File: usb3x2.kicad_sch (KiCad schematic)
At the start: 102 parts, among them J501 WE_632723300011_alt_symbol, J502 WE_632723300011_alt_symbol, Q501 BSS138W-7-F, Q502 BSS138W-7-F, U501 HD3SS3220, U502 HD3SS3220, U503 AP22615, U504 AP22615, U505 TPD4E05U06QDQARQ1, U506 TPD4E05U06QDQARQ1, U507 TPD4E05U06QDQARQ1, U508 TPD4E05U06QDQARQ1, U509 TPD4E05U06QDQARQ1, U510 TPD4E05U06QDQARQ1

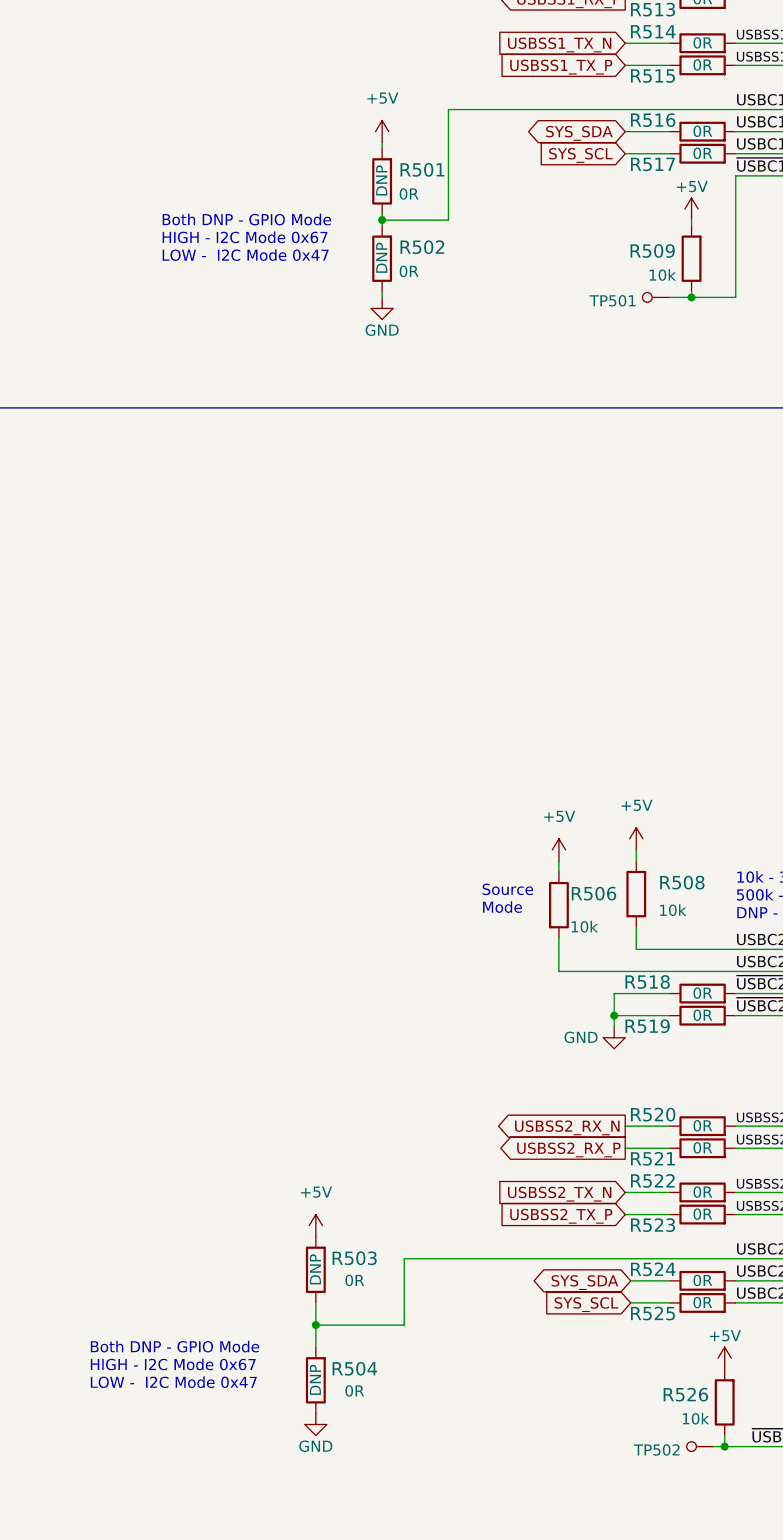
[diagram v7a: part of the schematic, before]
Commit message: Cleaned up the schematic, fixed library issues, annotated schematic
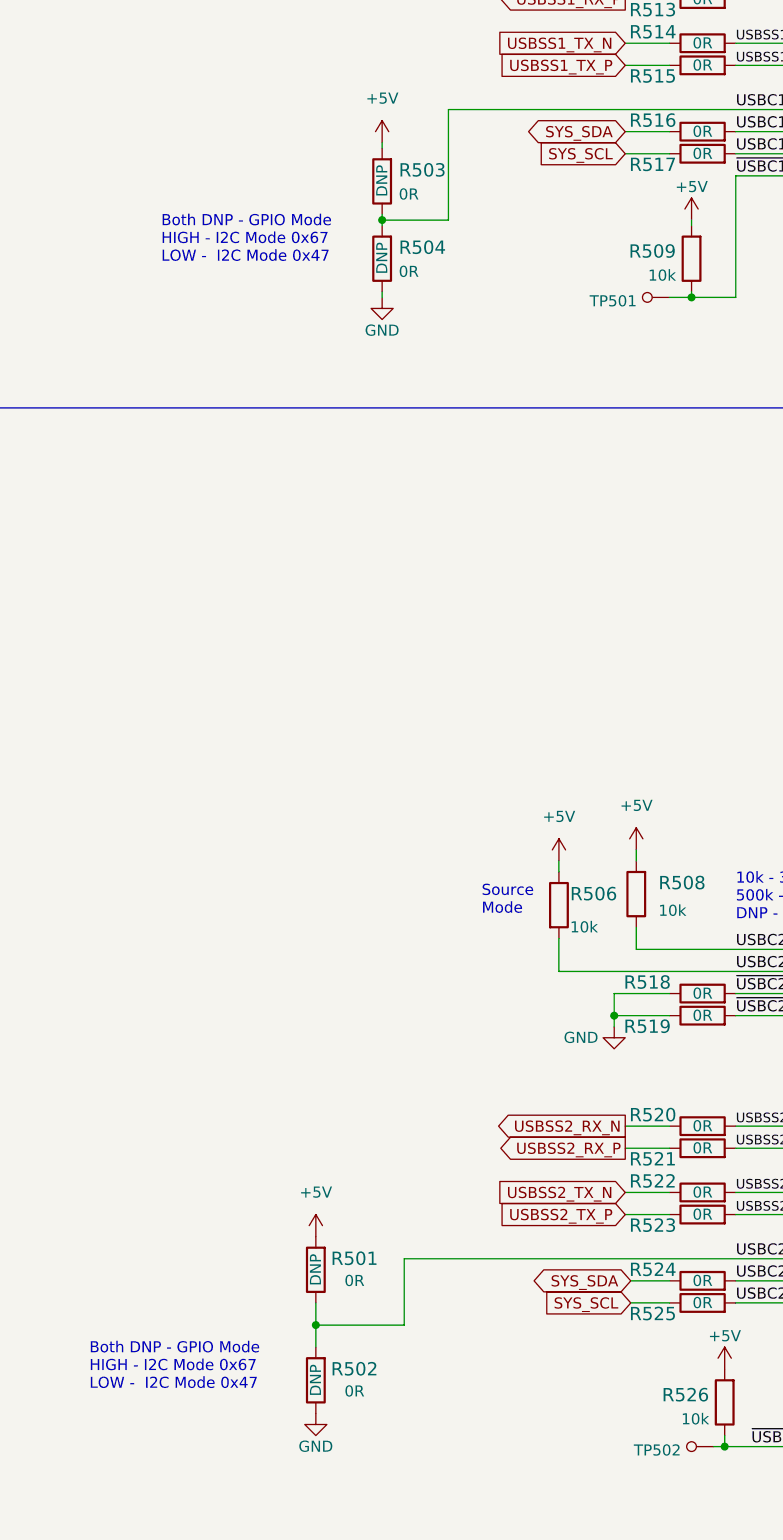
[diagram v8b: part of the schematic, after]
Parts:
- renumbered R503 to R501, R504 to R502, R501 to R503, R502 to R504
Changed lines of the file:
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@@
   (title_block
     (title "Jetson Orin NX Baseboard")
-    (date "2022-09-20")
+    (date "2022-09-28")
+    (rev "0.1.0")
     (company "Antmicro Ltd")
     (comment 1 "www.antmicro.com")
@@
     (pin "1")
   )
-  (symbol (lib_name "TPD4E05U06QDQARQ1_2") (lib_id "antmicroTVSDiodes:TPD4E05U06QDQARQ1") (at 255.27 262.89 270) (unit 1)
+  (symbol (lib_id "antmicroTVSDiodes:TPD4E05U06QDQARQ1") (at 255.27 262.89 270) (unit 1)
     (in_bom yes) (on_board yes)
     (property "Reference" "U508" (id 0) (at 264.16 264.7949 90)
@@
       (effects (font (size 1.27 1.27)) (justify left) hide)
     )
-    (property "Datasheet" "http://www.ti.com/general/docs/lit/getliterature.tsp?genericPartNumber=TPD4E001&fileType=pdf" (id 3) (at 265.43 262.89 0)
+    (property "Datasheet" "https://www.ti.com/lit/ds/symlink/tpd4e05u06-q1.pdf?HQS=dis-mous-null-mousermode-dsf-pf-null-wwe&ts=1663591265741&ref_url=https%253A%252F%252Fwww.mouser.pl%252F" (id 3) (at 265.43 262.89 0)
       (effects (font (size 1.27 1.27)) (justify left) hide)
     )
@@
     (pin "1")
   )
-  (symbol (lib_name "TPD4E05U06QDQARQ1_3") (lib_id "antmicroTVSDiodes:TPD4E05U06QDQARQ1") (at 228.6 262.89 270) (unit 1)
+  (symbol (lib_id "antmicroTVSDiodes:TPD4E05U06QDQARQ1") (at 228.6 262.89 270) (unit 1)
     (in_bom yes) (on_board yes)
     (property "Reference" "U506" (id 0) (at 237.49 264.7949 90)
@@
       (effects (font (size 1.27 1.27)) (justify left) hide)
     )
-    (property "Datasheet" "http://www.ti.com/general/docs/lit/getliterature.tsp?genericPartNumber=TPD4E001&fileType=pdf" (id 3) (at 238.76 262.89 0)
+    (property "Datasheet" "https://www.ti.com/lit/ds/symlink/tpd4e05u06-q1.pdf?HQS=dis-mous-null-mousermode-dsf-pf-null-wwe&ts=1663591265741&ref_url=https%253A%252F%252Fwww.mouser.pl%252F" (id 3) (at 238.76 262.89 0)
       (effects (font (size 1.27 1.27)) (justify left) hide)
     )
@@
   (symbol (lib_id "antmicroResistors0402:R_0R_0402") (at 71.12 131.445 90) (unit 1)
     (in_bom yes) (on_board yes)
-    (property "Reference" "R502" (id 0) (at 73.025 130.175 90)
+    (property "Reference" "R504" (id 0) (at 73.025 130.175 90)
       (effects (font (size 1.524 1.524)) (justify right))
     )
@@
   (symbol (lib_id "power:GND") (at 99.06 87.63 0) (unit 1)
     (in_bom yes) (on_board yes)
-    (property "Reference" "#PWR0507" (id 0) (at 99.06 93.98 0)
+    (property "Reference" "#PWR0508" (id 0) (at 99.06 93.98 0)
       (effects (font (size 1.27 1.27)) hide)
     )
@@
   (symbol (lib_id "power:GND") (at 71.12 135.89 0) (unit 1)
     (in_bom yes) (on_board yes)
-    (property "Reference" "#PWR0502" (id 0) (at 71.12 142.24 0)
+    (property "Reference" "#PWR0504" (id 0) (at 71.12 142.24 0)
       (effects (font (size 1.27 1.27)) hide)
     )
@@
     (pin "2")
   )
-  (symbol (lib_name "TPD4E05U06QDQARQ1_3") (lib_id "antmicroTVSDiodes:TPD4E05U06QDQARQ1") (at 228.6 130.81 270) (unit 1)
+  (symbol (lib_id "antmicroTVSDiodes:TPD4E05U06QDQARQ1") (at 228.6 130.81 270) (unit 1)
     (in_bom yes) (on_board yes)
     (property "Reference" "U505" (id 0) (at 237.49 132.7149 90)
@@
       (effects (font (size 1.27 1.27)) (justify left) hide)
     )
-    (property "Datasheet" "http://www.ti.com/general/docs/lit/getliterature.tsp?genericPartNumber=TPD4E001&fileType=pdf" (id 3) (at 238.76 130.81 0)
+    (property "Datasheet" "https://www.ti.com/lit/ds/symlink/tpd4e05u06-q1.pdf?HQS=dis-mous-null-mousermode-dsf-pf-null-wwe&ts=1663591265741&ref_url=https%253A%252F%252Fwww.mouser.pl%252F" (id 3) (at 238.76 130.81 0)
       (effects (font (size 1.27 1.27)) (justify left) hide)
     )
@@
     (pin "1")
   )
-  (symbol (lib_id "crosslink-nx-video-converter:GND") (at 289.56 194.31 0) (unit 1)
+  (symbol (lib_id "power:GND") (at 289.56 194.31 0) (unit 1)
     (in_bom yes) (on_board yes)
     (property "Reference" "#PWR0551" (id 0) (at 289.56 200.66 0)
@@
     )
     (property "Value" "GND" (id 1) (at 289.56 198.12 0))
-    (property "Footprint" "crosslink-nx-video-converter-footprints:" (id 2) (at 289.56 194.31 0)
+    (property "Footprint" "" (id 2) (at 289.56 194.31 0)
       (effects (font (size 1.27 1.27)) hide)
     )
@@
     (pin "2")
   )
-  (symbol (lib_name "TPD4E05U06QDQARQ1_2") (lib_id "antmicroTVSDiodes:TPD4E05U06QDQARQ1") (at 255.27 130.81 270) (unit 1)
+  (symbol (lib_id "antmicroTVSDiodes:TPD4E05U06QDQARQ1") (at 255.27 130.81 270) (unit 1)
     (in_bom yes) (on_board yes)
     (property "Reference" "U507" (id 0) (at 264.16 132.7149 90)
@@
       (effects (font (size 1.27 1.27)) (justify left) hide)
     )
-    (property "Datasheet" "http://www.ti.com/general/docs/lit/getliterature.tsp?genericPartNumber=TPD4E001&fileType=pdf" (id 3) (at 265.43 130.81 0)
+    (property "Datasheet" "https://www.ti.com/lit/ds/symlink/tpd4e05u06-q1.pdf?HQS=dis-mous-null-mousermode-dsf-pf-null-wwe&ts=1663591265741&ref_url=https%253A%252F%252Fwww.mouser.pl%252F" (id 3) (at 265.43 130.81 0)
       (effects (font (size 1.27 1.27)) (justify left) hide)
     )
@@
   (symbol (lib_id "power:+5V") (at 71.12 118.11 0) (unit 1)
     (in_bom yes) (on_board yes) (fields_autoplaced)
-    (property "Reference" "#PWR0501" (id 0) (at 71.12 121.92 0)
+    (property "Reference" "#PWR0503" (id 0) (at 71.12 121.92 0)
       (effects (font (size 1.27 1.27)) hide)
     )
@@
   (symbol (lib_id "power:+5V") (at 63.5 243.84 0) (unit 1)
     (in_bom yes) (on_board yes) (fields_autoplaced)
-    (property "Reference" "#PWR0503" (id 0) (at 63.5 247.65 0)
+    (property "Reference" "#PWR0501" (id 0) (at 63.5 247.65 0)
       (effects (font (size 1.27 1.27)) hide)
     )
@@
   (symbol (lib_id "antmicroResistors0402:R_0R_0402") (at 71.12 122.555 90) (unit 1)
     (in_bom yes) (on_board yes)
-    (property "Reference" "R501" (id 0) (at 73.025 121.285 90)
+    (property "Reference" "R503" (id 0) (at 73.025 121.285 90)
       (effects (font (size 1.524 1.524)) (justify right))
     )
@@
     (pin "2")
   )
-  (symbol (lib_id "crosslink-nx-video-converter:GND") (at 289.56 62.23 0) (unit 1)
+  (symbol (lib_id "power:GND") (at 289.56 62.23 0) (unit 1)
     (in_bom yes) (on_board yes)
     (property "Reference" "#PWR0550" (id 0) (at 289.56 68.58 0)
@@
     )
     (property "Value" "GND" (id 1) (at 289.56 66.04 0))
-    (property "Footprint" "crosslink-nx-video-converter-footprints:" (id 2) (at 289.56 62.23 0)
+    (property "Footprint" "" (id 2) (at 289.56 62.23 0)
       (effects (font (size 1.27 1.27)) hide)
     )
@@
   (symbol (lib_id "antmicroResistors0402:R_0R_0402") (at 63.5 260.35 90) (unit 1)
     (in_bom yes) (on_board yes)
-    (property "Reference" "R504" (id 0) (at 67.945 259.08 90)
+    (property "Reference" "R502" (id 0) (at 67.945 259.08 90)
       (effects (font (size 1.524 1.524)))
     )
@@
   (symbol (lib_id "antmicroResistors0402:R_0R_0402") (at 63.5 247.65 90) (unit 1)
     (in_bom yes) (on_board yes)
-    (property "Reference" "R503" (id 0) (at 67.945 246.38 90)
+    (property "Reference" "R501" (id 0) (at 67.945 246.38 90)
       (effects (font (size 1.524 1.524)))
     )
@@
     (pin "1")
   )
-  (symbol (lib_name "TPD4E05U06QDQARQ1_1") (lib_id "antmicroTVSDiodes:TPD4E05U06QDQARQ1") (at 256.54 68.58 270) (mirror x) (unit 1)
+  (symbol (lib_id "antmicroTVSDiodes:TPD4E05U06QDQARQ1") (at 256.54 68.58 270) (mirror x) (unit 1)
     (in_bom yes) (on_board yes)
     (property "Reference" "U509" (id 0) (at 264.16 66.04 90)
@@
       (effects (font (size 1.27 1.27)) (justify left) hide)
     )
-    (property "Datasheet" "http://www.ti.com/general/docs/lit/getliterature.tsp?genericPartNumber=TPD4E001&fileType=pdf" (id 3) (at 266.7 68.58 0)
+    (property "Datasheet" "https://www.ti.com/lit/ds/symlink/tpd4e05u06-q1.pdf?HQS=dis-mous-null-mousermode-dsf-pf-null-wwe&ts=1663591265741&ref_url=https%253A%252F%252Fwww.mouser.pl%252F" (id 3) (at 266.7 68.58 0)
       (effects (font (size 1.27 1.27)) (justify left) hide)
     )
@@
   (symbol (lib_id "power:GND") (at 97.79 219.71 0) (unit 1)
     (in_bom yes) (on_board yes)
-    (property "Reference" "#PWR0508" (id 0) (at 97.79 226.06 0)
+    (property "Reference" "#PWR0507" (id 0) (at 97.79 226.06 0)
       (effects (font (size 1.27 1.27)) hide)
     )
@@
     (pin "2")
   )
-  (symbol (lib_name "TPD4E05U06QDQARQ1_1") (lib_id "antmicroTVSDiodes:TPD4E05U06QDQARQ1") (at 256.54 200.66 270) (mirror x) (unit 1)
+  (symbol (lib_id "antmicroTVSDiodes:TPD4E05U06QDQARQ1") (at 256.54 200.66 270) (mirror x) (unit 1)
     (in_bom yes) (on_board yes)
     (property "Reference" "U510" (id 0) (at 264.16 198.12 90)
@@
       (effects (font (size 1.27 1.27)) (justify left) hide)
     )
-    (property "Datasheet" "http://www.ti.com/general/docs/lit/getliterature.tsp?genericPartNumber=TPD4E001&fileType=pdf" (id 3) (at 266.7 200.66 0)
+    (property "Datasheet" "https://www.ti.com/lit/ds/symlink/tpd4e05u06-q1.pdf?HQS=dis-mous-null-mousermode-dsf-pf-null-wwe&ts=1663591265741&ref_url=https%253A%252F%252Fwww.mouser.pl%252F" (id 3) (at 266.7 200.66 0)
       (effects (font (size 1.27 1.27)) (justify left) hide)
     )
@@
   (symbol (lib_id "power:GND") (at 63.5 264.16 0) (unit 1)
     (in_bom yes) (on_board yes)
-    (property "Reference" "#PWR0504" (id 0) (at 63.5 270.51 0)
+    (property "Reference" "#PWR0502" (id 0) (at 63.5 270.51 0)
       (effects (font (size 1.27 1.27)) hide)
     )
